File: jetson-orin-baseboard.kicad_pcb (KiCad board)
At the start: 2 copper layers, 447 parts, among them J1 533980471, J10 532611071, J11 ERF8-020-05.0-S-DV-L-TR, J12 Molex_Nano-Fit-105430_xx02-ho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, J13 SIM8066-6-1-14-01-A, J14 SIM7600X-M2-B, J2 1-2199230-6, J3 WE_632723300011_alt_symbol, J4 WE_632723300011_alt_symbol, J5 ARJM11C7-502-AB-ER2-T, J6 F32R-1A7H1-11022, J7 F32R-1A7H1-11022, J8 TC2050-IDC-NL, J9 533980471, M1 jetson-orin-nx/nano-module, M2 M2_2280, Q1 PJE138K, Q10 PJE138K, Q11 PJE138K, Q12 PJE138K, Q13 SSM3J332R, Q2 PJE138K, Q3 PJE138K, Q4 PJE138K, Q5 PJE138K, Q6 BCM857BS-7-F, Q7 PJE138K, Q8 SSM3J332R, Q9 SSM3J332R, SW1 PCM12SMTR, U1 NTS0102GT, U10 TPD4E05U06QDQARQ1, U11 TPD4E05U06QDQARQ1, U12 HD3SS3220, U13 AP22615, U14 TPD4E05U06QDQARQ1, U15 TPD4E05U06QDQARQ1, U16 TPD4E05U06QDQARQ1, U17 TS3USB30ERSWR, U18 SN74LV1T125DCKR, U19 SN74LV1T125DCKR, U2 TPS65987, U20 NTS0102GT, U21 ICM-20602, U22 74LVC2G14GV, U23 74LVC1G175GV, U24 TPS56C230, U25 TPS56C230, U26 NCP730BMT330TBG, U27 TPS7A0518PDBVT, U3 W25Q80DVUXIE_TR, U4 NCP730BMT330TBG, U5 FT230XQ-R, U6 TUSB1046-DCI, U7 TPD4E05U06QDQARQ1, U8 AP22615, U9 TPD4E05U06QDQARQ1, Y1 ECS-327MVATX-2-CN-TR3

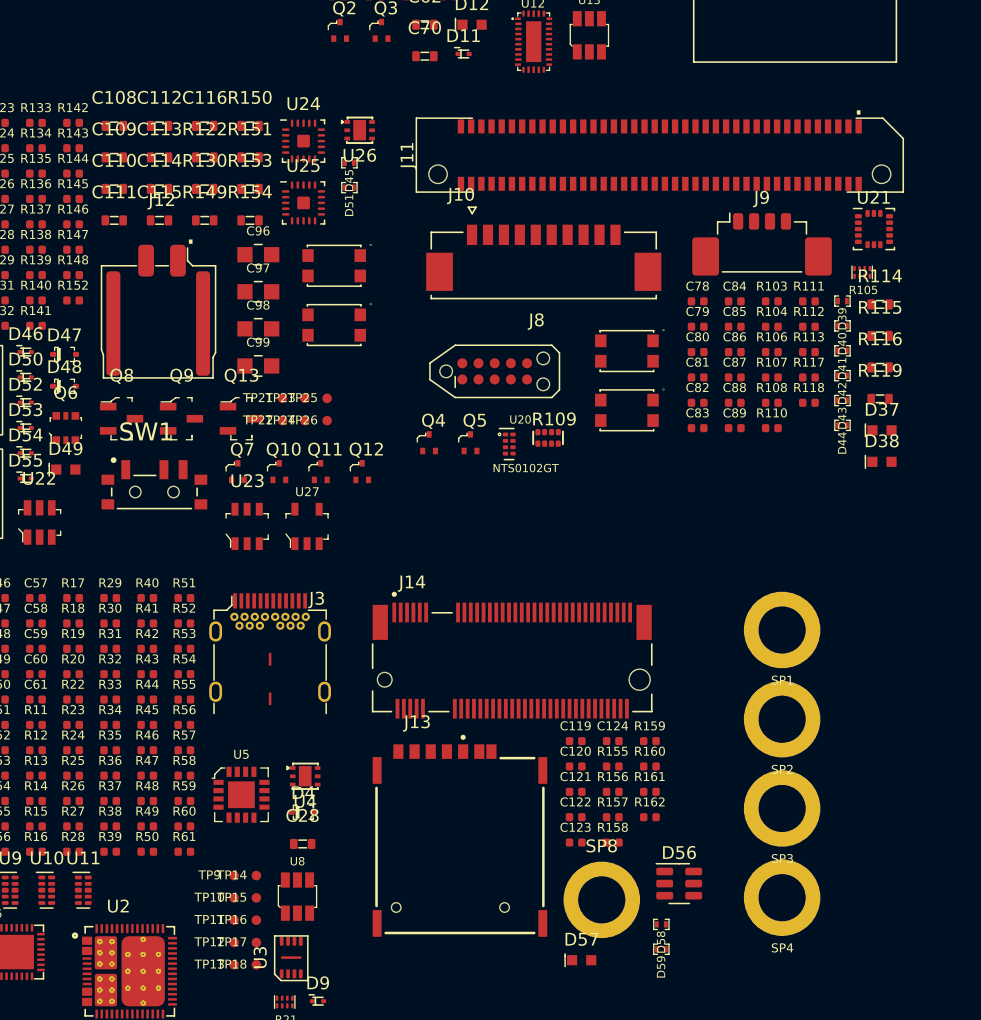
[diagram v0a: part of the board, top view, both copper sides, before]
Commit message: Footprints well assigned, XT30 added, Shields grounded
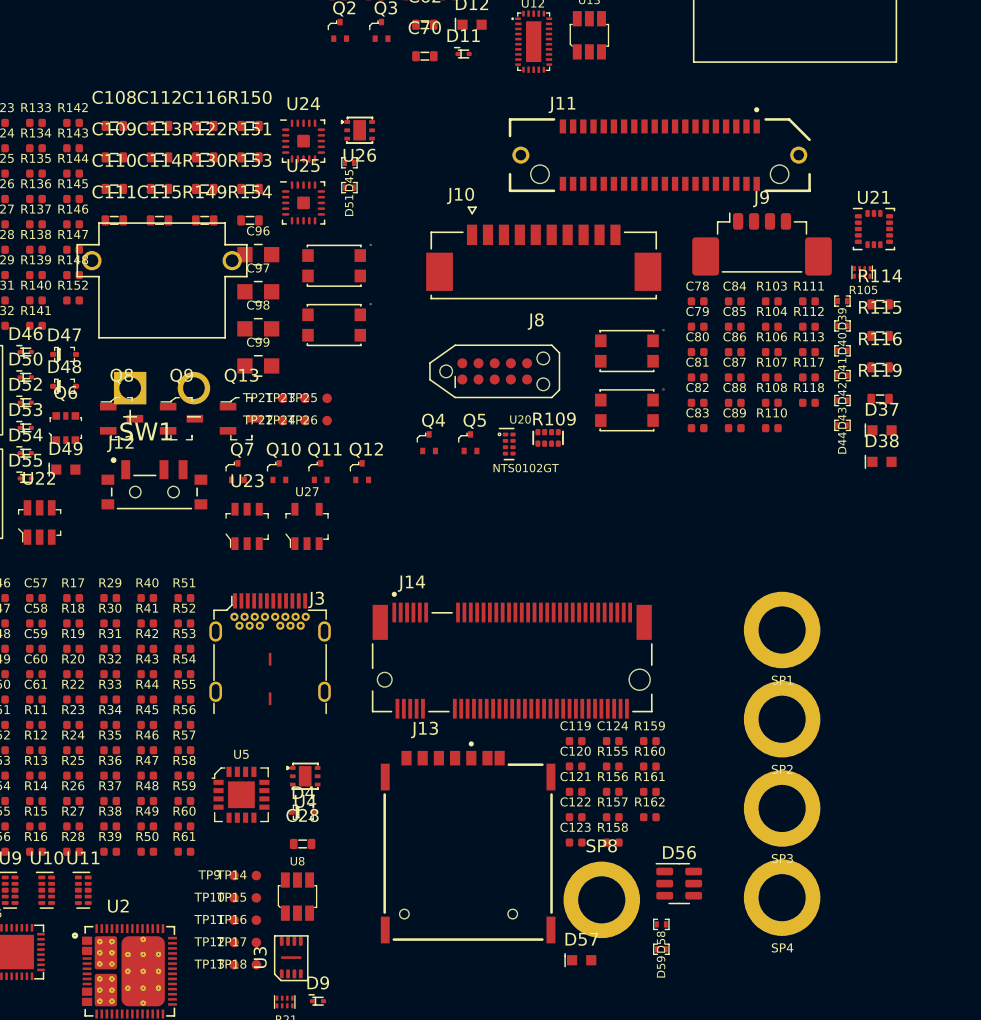
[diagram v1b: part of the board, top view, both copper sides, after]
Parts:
- J11: footprint jetson-orin-baseboard-footprints:ERF8-040-XX.X-X-DV-XX -> jetson-orin-baseboard-footprints:SAMTEC_ERF8-020-05.0-S-DV-L-TR
- J12: value Molex_Nano-Fit-105430_xx02-horizontal -> XT30PW-M; footprint jetson-orin-baseboard-footprints:Molex_Nano-Fit_105430-xx02_1x02_P2.50mm_Horizontal_SMD -> jetson-orin-baseboard-footprints:AMASS_XT30PW-M
- J13: value SIM8066-6-1-14-01-A -> SIM8066-6-1-14-01-A_REVA
- moved M1 2.65 mm to (157.5, 48.3)
- moved J13 0.82 mm to (180.3, 129.5)
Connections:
- D13 pad A: (no net) -> GND
- D13 pad K: (no net) -> CSI0_D0_N
- D14 pad A: (no net) -> GND
- D14 pad K: (no net) -> CSI2_D0_N
- D15 pad A: (no net) -> GND
- D15 pad K: (no net) -> CSI0_D0_P
- D16 pad A: (no net) -> GND
- D16 pad K: (no net) -> CSI2_D0_P
- D17 pad A: (no net) -> GND
- D17 pad K: (no net) -> CSI0_D1_N
- D18 pad A: (no net) -> GND
- D18 pad K: (no net) -> CSI2_D1_N
- D19 pad A: (no net) -> GND
- D19 pad K: (no net) -> CSI0_D1_P
- D20 pad A: (no net) -> GND
- D20 pad K: (no net) -> CSI2_D1_P
- D21 pad A: (no net) -> GND
- D21 pad K: (no net) -> CSI0_CLK_N
- D22 pad A: (no net) -> GND
- D22 pad K: (no net) -> CSI2_CLK_N
- D23 pad A: (no net) -> GND
- D23 pad K: (no net) -> CSI0_CLK_P
- D24 pad A: (no net) -> GND
- D24 pad K: (no net) -> CSI2_CLK_P
- D25 pad A: (no net) -> GND
- D25 pad K: (no net) -> CSI1_D0_N
- D26 pad A: (no net) -> GND
- D26 pad K: (no net) -> CSI3_D0_N
- D27 pad A: (no net) -> GND
- D27 pad K: (no net) -> CSI1_D0_P
- D28 pad A: (no net) -> GND
- D28 pad K: (no net) -> CSI3_D0_P
- D29 pad A: (no net) -> GND
- D29 pad K: (no net) -> CSI1_D1_N
- D30 pad A: (no net) -> GND
- D30 pad K: (no net) -> CSI3_D1_N
- D31 pad A: (no net) -> GND
- D31 pad K: (no net) -> CSI1_D1_P
- D32 pad A: (no net) -> GND
- D32 pad K: (no net) -> CSI3_D1_P
- D33 pad A: (no net) -> GND
- D33 pad K: (no net) -> Net-(D33-PadK)
- D34 pad A: (no net) -> GND
- D34 pad K: (no net) -> Net-(D34-PadK)
- D35 pad A: (no net) -> GND
- D35 pad K: (no net) -> CAM0_MCLK
- D36 pad A: (no net) -> GND
- D36 pad K: (no net) -> CAM1_MCLK
- J13 pad C1: (no net) -> Net-(D56-IO2)
- J13 pad C2: (no net) -> Net-(J13-RST)
- J13 pad C3: (no net) -> Net-(J13-CLK)
- J13 pad C5: (no net) -> GND
- J13 pad C6: (no net) -> unconnected-(J13-VPP-PadC6)
- J13 pad C7: (no net) -> Net-(J13-I/O)
- J13 pad CD: (no net) -> Net-(J13-PadCD)
- J13 pad G1: (no net) -> GND
- J13 pad G2: (no net) -> GND
- J13 pad G3: (no net) -> GND
- J13 pad G4: (no net) -> GND
- J14 pad S1: (no net) -> GND
- J14 pad S2: (no net) -> GND
- J5 pad L1: (no net) -> +3V3
- J5 pad L2: (no net) -> Net-(J5-LED_GRN-)
- J5 pad L3: (no net) -> +3V3
- J5 pad L4: (no net) -> Net-(J5-LED_YEL-)
- J5 pad S1: (no net) -> Net-(J5-SHIELD1)
- J5 pad S2: (no net) -> Net-(J5-SHIELD1)
- J6 pad 6: Net-(D33-K) -> Net-(D33-PadK)
- J6 pad S1: (no net) -> GND
- J6 pad S2: (no net) -> GND
- J7 pad 6: Net-(D34-K) -> Net-(D34-PadK)
- J7 pad S1: (no net) -> GND
- J7 pad S2: (no net) -> GND
- R155 pad 1: Net-(J13-CD) -> Net-(J13-PadCD)
- U18 pad 4: Net-(D33-K) -> Net-(D33-PadK)
- U19 pad 4: Net-(D34-K) -> Net-(D34-PadK)
- U2 pad 1: unconnected-(U2B-PP_HV2-Pad1) -> GND
- U2 pad 11: unconnected-(U2B-PP_HV1-Pad11) -> USBPD_HV
- U2 pad 13: unconnected-(U2B-VBUS1-Pad13) -> /USB Debug, DP/USBC0_VBUS
- U2 pad 24: unconnected-(U2B-C_CC1-Pad24) -> /USB Debug, DP/USBC0_CC1
- U2 pad 25: unconnected-(U2B-PP_CABLE-Pad25) -> +5V
- U2 pad 26: unconnected-(U2B-C_CC2-Pad26) -> /USB Debug, DP/USBC0_CC2
- U2 pad 3: unconnected-(U2B-VBUS2-Pad3) -> /USB Debug, DP/USBC0_VBUS
- U2 pad 52: Net-(U2B-DRAIN2-Pad52) -> Net-(U2B-DRAIN1-Pad15)
- U2 pad 56: Net-(U2B-DRAIN2-Pad52) -> Net-(U2B-DRAIN1-Pad15)
- U2 pad 57: Net-(U2B-DRAIN2-Pad52) -> Net-(U2B-DRAIN1-Pad15)
- U2 pad 7: Net-(U2B-DRAIN2-Pad52) -> Net-(U2B-DRAIN1-Pad15)
- U3 pad EP: (no net) -> GND

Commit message: Starting PCB Design
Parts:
- added REF**: m2_3142, jetson-orin-baseboard-footprints:m2_3142, F.Cu at (236.0, 171.1)
- J2: value 1-2199230-6 -> CONN_1-2199230-6
- SW1: value PCM12SMTR -> SW_PCM12SMTR
- moved D13 204.0 mm to (13.4, 119.6), turned to 180 degrees
- moved D15 199.5 mm to (15.9, 119.6)
- moved D21 198.3 mm to (22.0, 119.6), turned to 180 degrees
- moved D27 196.5 mm to (28.8, 119.6)
- moved D17 195.7 mm to (17.7, 119.6), turned to 180 degrees
- moved D23 193.8 mm to (24.5, 119.6)
- moved D29 192.5 mm to (30.6, 119.6), turned to 180 degrees
- moved D19 191.3 mm to (20.2, 119.6)
- moved D35 190.7 mm to (37.4, 119.6)
- moved D25 190.0 mm to (26.3, 119.6), turned to 180 degrees
- moved D31 188.1 mm to (33.1, 119.6)
- moved U18 185.1 mm to (34.3, 123.5), turned to 90 degrees
- moved D33 184.2 mm to (34.9, 119.6), turned to 180 degrees
- moved R99 182.0 mm to (36.2, 129.0)
- moved R100 181.5 mm to (36.2, 130.1)
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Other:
- copper layers 2 -> 8

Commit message: Resetting PCB
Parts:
- moved TP26 321.1 mm to (35.8, 304.9)
- moved C98 321.0 mm to (34.2, 299.3), turned to 180 degrees
- moved R152 317.4 mm to (35.0, 307.8)
- moved C96 317.4 mm to (34.2, 297.6), turned to 180 degrees
- moved R136 317.0 mm to (38.5, 305.4)
- moved R142 311.3 mm to (39.8, 300.7)
- moved L2 311.3 mm to (36.1, 278.7)
- moved C106 310.7 mm to (35.7, 267.8)
- moved C112 310.7 mm to (45.9, 273.4)
- moved C90 310.7 mm to (51.8, 329.2)
- moved C91 310.7 mm to (40.9, 322.8)
- moved C93 310.7 mm to (37.1, 325.2)
- moved C99 310.7 mm to (29.1, 273.7)
- moved D52 310.7 mm to (45.5, 300.9)
- moved D53 310.7 mm to (50.3, 269.3)
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
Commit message: Camera interface placement
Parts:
- moved U18 273.7 mm to (257.5, 21.6), turned to 0 degrees
- moved C77 271.5 mm to (256.5, 17.5), turned to 180 degrees
- moved D33 270.1 mm to (261.6, 21.3), turned to -90 degrees
- moved D31 268.3 mm to (261.6, 23.1), turned to 90 degrees
- moved D29 265.9 mm to (261.6, 25.6), turned to -90 degrees
- moved D27 264.2 mm to (261.6, 27.4), turned to 90 degrees
- moved D25 261.8 mm to (261.6, 29.9), turned to -90 degrees
- moved D23 260.1 mm to (261.6, 31.7), turned to 90 degrees
- moved D21 257.8 mm to (261.6, 34.2), turned to -90 degrees
- moved D19 256.1 mm to (261.6, 36.0), turned to 90 degrees
- moved D17 253.8 mm to (261.6, 38.5), turned to -90 degrees
- moved J6 253.0 mm to (271.8, 32.8), turned to -90 degrees
- moved D15 252.2 mm to (261.6, 40.3), turned to 90 degrees
- moved D13 246.7 mm to (261.6, 46.1), turned to -90 degrees
- moved U19 244.1 mm to (257.5, 51.5), turned to 0 degrees
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
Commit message: Edge Cuts & Holes setup like original Antmicro Jetson Orin Baseboard
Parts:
- removed M1: jetson-orin-nx/nano-module, jetson-orin-baseboard-footprints:jetson-orin-nx-nano-module
- removed REF**: m2_3142, jetson-orin-baseboard-footprints:m2_3142
- J2: value CONN_1-2199230-6 -> 1-2199230-6
- SW1: value SW_PCM12SMTR -> PCM12SMTR
- moved SP1 310.3 mm to (67.5, 45.7)
- moved SP2 286.2 mm to (168.2, 44.5)
- moved SP3 284.2 mm to (64.6, 91.6)
- moved SP4 252.0 mm to (170.6, 92.8)
- moved SP6 186.0 mm to (147.9, 90.4)
- moved SP5 174.2 mm to (84.3, 90.4)
- moved R130 147.8 mm to (24.0, 249.8), turned to 180 degrees
- moved D54 38.4 mm to (178.8, 277.7)
- moved A1 36.3 mm to (89.2, 76.1)
- moved C107 33.4 mm to (181.4, 292.6)
- moved C60 33.4 mm to (171.1, 380.6)
- moved C61 33.4 mm to (172.3, 380.7)
- moved D10 33.4 mm to (173.7, 385.2)
- moved D9 33.4 mm to (169.6, 380.6)
- moved R61 33.4 mm to (173.7, 380.6)
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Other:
- board outline added: 120 x 60 mm

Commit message: Text size changes and positioning important components part 1
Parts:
- removed R100, R101, R102, R99: 1k, jetson-orin-baseboard-footprints:0402-res
- added R163: 4x1000R_0402_array, jetson-orin-baseboard-footprints:R_Array_4x0402, F.Cu at (155.8, 105.6)
- BAT1, C10, C11, C12, C13, C14, C15, C16, C17, C18, C19, C20, C21, C22, C78, C80, D3, J2, J8, M2, R1, R10, R105, R6, R7, R8, R9, SP7, U2, U20, Y1: moved to B.Cu
- moved C103 304.7 mm to (261.6, 87.7)
- moved C105 304.7 mm to (259.0, 87.7)
- moved C106 304.7 mm to (257.9, 59.5)
- moved C109 304.7 mm to (266.3, 75.8)
- moved C112 304.7 mm to (268.2, 65.0)
- moved C115 304.7 mm to (266.3, 78.1)
- moved L2 304.7 mm to (258.3, 70.3)
- moved R137 304.7 mm to (264.2, 89.2)
- moved R138 304.7 mm to (264.2, 90.1)
- moved R139 304.7 mm to (263.3, 60.4)
- moved R140 304.7 mm to (263.3, 59.3)
- moved R145 304.7 mm to (263.8, 91.5)
- moved R146 304.7 mm to (264.8, 62.2)
- moved R147 304.7 mm to (262.6, 62.2)
- moved R152 304.7 mm to (257.2, 99.5)
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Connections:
- J11 pad 08: /Peripherals/UART1_TXD_CONN -> /Peripherals/IO4
- J11 pad 10: /Peripherals/UART1_RXD_CONN -> /Peripherals/IO5
- J11 pad 19: /Peripherals/IO4 -> /Peripherals/UART1_TXD_CONN
- J11 pad 21: /Peripherals/IO5 -> /Peripherals/UART1_RXD_CONN

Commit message: Putting SSD right place and buck component placements
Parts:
- C103, C104, C97, C98, C99, R137, R138, R139, R140, R142, R143, TP23: moved to B.Cu
- moved D53 216.5 mm to (57.9, 88.5), turned to 180 degrees
- moved C114 215.9 mm to (57.3, 92.7), turned to 180 degrees
- moved C110 215.7 mm to (57.3, 89.7), turned to 180 degrees
- moved C112 212.5 mm to (57.3, 91.2), turned to 180 degrees
- moved R150 211.5 mm to (59.5, 91.0), turned to 90 degrees
- moved C116 209.7 mm to (57.3, 94.2), turned to 180 degrees
- moved R146 205.9 mm to (61.4, 93.6), turned to 0 degrees
- moved R140 204.8 mm to (62.0, 96.4)
- moved R147 203.5 mm to (61.4, 92.6), turned to 180 degrees
- moved R139 202.8 mm to (63.5, 95.4), turned to 180 degrees
- moved R141 202.1 mm to (62.1, 90.2), turned to -90 degrees
- moved L2 200.6 mm to (59.8, 98.8), turned to 180 degrees
- moved R143 199.4 mm to (63.6, 94.5), turned to 180 degrees
- moved C104 199.0 mm to (65.1, 94.9), turned to 90 degrees
- moved U25 197.7 mm to (64.5, 93.2), turned to 180 degrees
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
